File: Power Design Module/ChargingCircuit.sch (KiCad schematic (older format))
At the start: 21 parts, among them J4 USB_B_Micro, J5 Battery Output, SW1 Charge Disable Switch, SW2 Input Current Selection, U3 BQ24072TRGTR

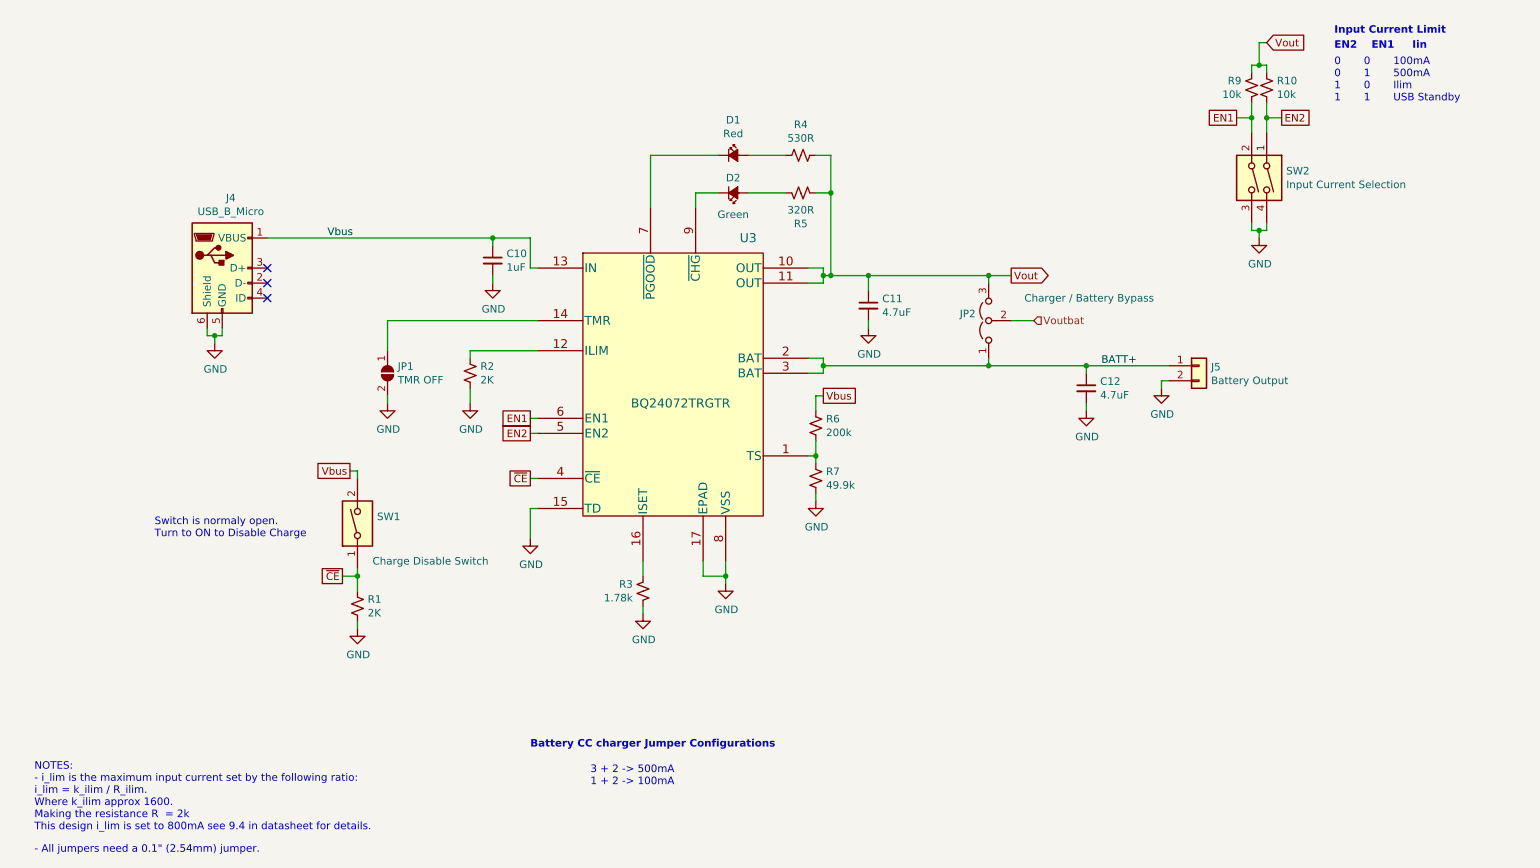
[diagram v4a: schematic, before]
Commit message: Final Power Breakout completed. Headers were used instead of the previous Molex Connectors
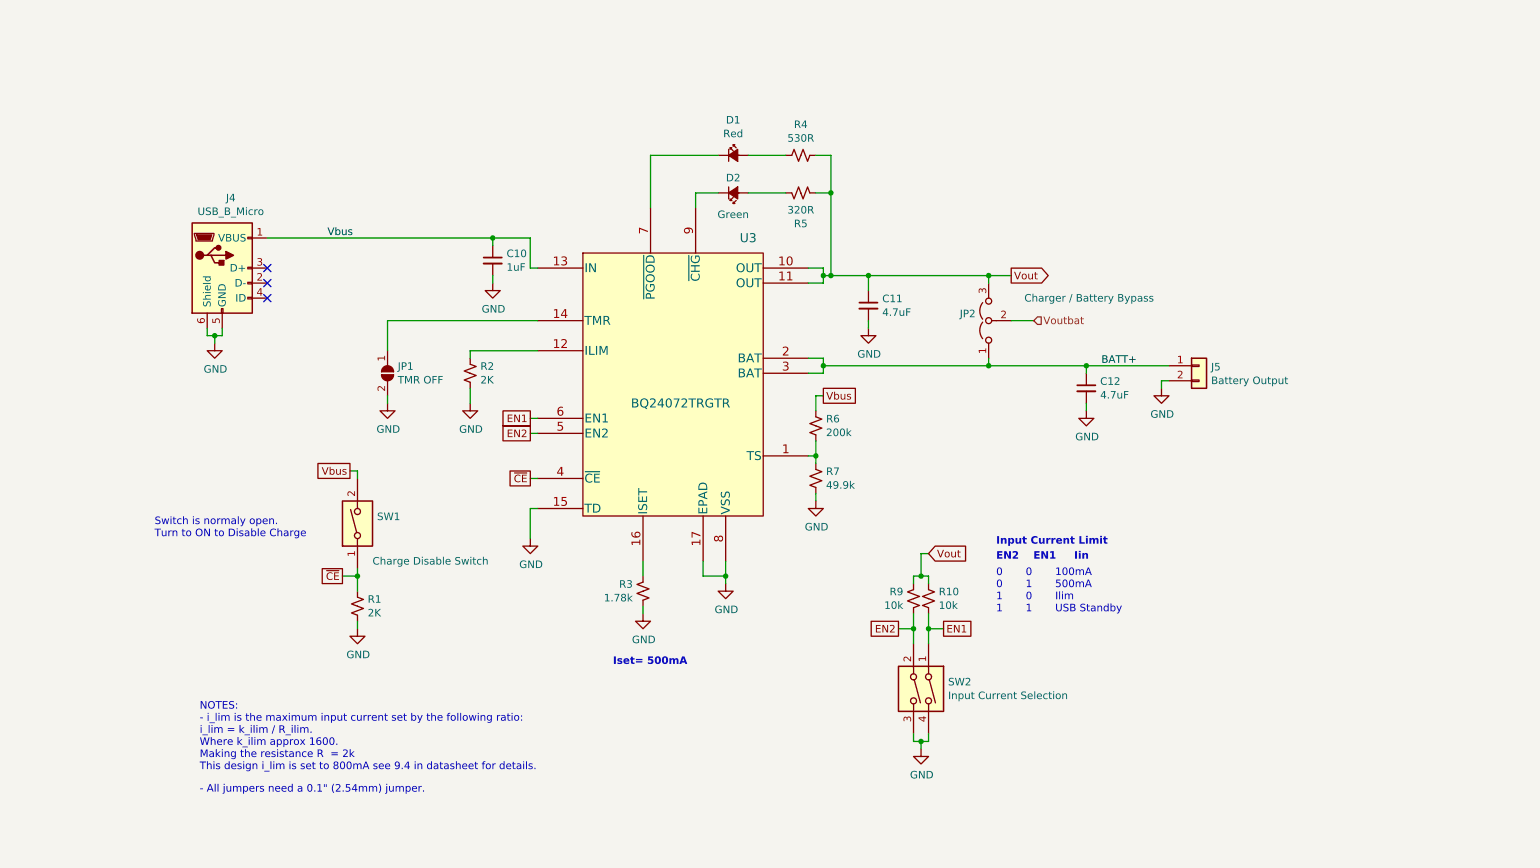
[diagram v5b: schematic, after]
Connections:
- net EN1: now also R10.2, SW2.1; no longer R9.1, SW2.2
- net EN2: now also R9.1, SW2.2; no longer R10.2, SW2.1
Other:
- note added: "Iset= 500mA\n"
- note removed: "3 + 2 -> 500mA\n1 + 2 -> 100mA"
- note removed: "Battery CC charger Jumper Configurations"
- moved on the sheet: R10, R9, SW2
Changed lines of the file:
@@
 $EndComp
-Wire Wire Line
-	5350 2100 5350 2000
-Wire Wire Line
-	5350 2000 5500 2000
 Wire Wire Line
 	5500 1750 5050 1750
@@
 L Switch:SW_DIP_x02 SW2
 U 1 1 5E2D5AAA
-P 9050 1900
-F 0 "SW2" V 9004 2130 50  0000 L CNN
-F 1 "Input Current Selection" V 9095 2130 50  0000 L CNN
-F 2 "Button_Switch_SMD:SW_DIP_SPSTx02_Slide_Copal_CHS-02B_W7.62mm_P1.27mm" H 9050 1900 50  0001 C CNN
-F 3 "~" H 9050 1900 50  0001 C CNN
-F 4 "CVS-02TB" H 9050 1900 50  0001 C CNN "Manfacturing #"
-	1    9050 1900
+P 6800 5300
+F 0 "SW2" V 6754 5530 50  0000 L CNN
+F 1 "Input Current Selection" V 6845 5530 50  0000 L CNN
+F 2 "Button_Switch_SMD:SW_DIP_SPSTx02_Slide_Copal_CHS-02B_W7.62mm_P1.27mm" H 6800 5300 50  0001 C CNN
+F 3 "~" H 6800 5300 50  0001 C CNN
+F 4 "CVS-02TB" H 6800 5300 50  0001 C CNN "Manfacturing #"
+	1    6800 5300
 	0    1    1    0
 $EndComp
-Text GLabel 9150 1000 2    50   Input ~ 0
+Text GLabel 6900 4400 2    50   Input ~ 0
 Vout
-Text GLabel 8950 1500 0    50   UnSpc ~ 0
+Text GLabel 7000 4900 2    50   UnSpc ~ 0
 EN1
-Text GLabel 9250 1500 2    50   UnSpc ~ 0
+Text GLabel 6700 4900 0    50   UnSpc ~ 0
 EN2
 $Comp
 L Device:R_Small_US R9
 U 1 1 5E2E11CE
-P 9050 1300
-F 0 "R9" H 8982 1254 50  0000 R CNN
-F 1 "10k" H 8982 1345 50  0000 R CNN
-F 2 "Resistor_SMD:R_0603_1608Metric_Pad1.05x0.95mm_HandSolder" H 9050 1300 50  0001 C CNN
-F 3 "~" H 9050 1300 50  0001 C CNN
-F 4 "SG73G1JTTD1002D" H 9050 1300 50  0001 C CNN "Manfacturing #"
-	1    9050 1300
+P 6800 4700
+F 0 "R9" H 6732 4654 50  0000 R CNN
+F 1 "10k" H 6732 4745 50  0000 R CNN
+F 2 "Resistor_SMD:R_0603_1608Metric_Pad1.05x0.95mm_HandSolder" H 6800 4700 50  0001 C CNN
+F 3 "~" H 6800 4700 50  0001 C CNN
+F 4 "SG73G1JTTD1002D" H 6800 4700 50  0001 C CNN "Manfacturing #"
+	1    6800 4700
 	1    0    0    1
 $EndComp
@@
 L Device:R_Small_US R10
 U 1 1 5E2E2CB5
-P 9150 1300
-F 0 "R10" H 9218 1346 50  0000 L CNN
-F 1 "10k" H 9218 1255 50  0000 L CNN
-F 2 "Resistor_SMD:R_0603_1608Metric_Pad1.05x0.95mm_HandSolder" H 9150 1300 50  0001 C CNN
-F 3 "~" H 9150 1300 50  0001 C CNN
-F 4 "SG73G1JTTD1002D" H 9150 1300 50  0001 C CNN "Manfacturing #"
-	1    9150 1300
-	1    0    0    -1
-$EndComp
-Wire Wire Line
-	9050 1400 9050 1500
-Wire Wire Line
-	9050 1500 8950 1500
-Wire Wire Line
-	9050 1500 9050 1600
-Connection ~ 9050 1500
-Wire Wire Line
-	9150 1400 9150 1500
-Wire Wire Line
-	9250 1500 9150 1500
-Connection ~ 9150 1500
-Wire Wire Line
-	9150 1500 9150 1600
-Wire Wire Line
-	9050 1200 9050 1150
-Wire Wire Line
-	9050 1150 9100 1150
-Wire Wire Line
-	9150 1150 9150 1200
-Wire Wire Line
-	9150 1000 9100 1000
-Wire Wire Line
-	9100 1000 9100 1150
-Connection ~ 9100 1150
-Wire Wire Line
-	9100 1150 9150 1150
-Wire Wire Line
-	9050 2200 9050 2250
-Wire Wire Line
-	9050 2250 9100 2250
-Wire Wire Line
-	9150 2250 9150 2200
-Wire Wire Line
-	9100 2250 9100 2300
-Connection ~ 9100 2250
-Wire Wire Line
-	9100 2250 9150 2250
+P 6900 4700
+F 0 "R10" H 6968 4746 50  0000 L CNN
+F 1 "10k" H 6968 4655 50  0000 L CNN
+F 2 "Resistor_SMD:R_0603_1608Metric_Pad1.05x0.95mm_HandSolder" H 6900 4700 50  0001 C CNN
+F 3 "~" H 6900 4700 50  0001 C CNN
+F 4 "SG73G1JTTD1002D" H 6900 4700 50  0001 C CNN "Manfacturing #"
+	1    6900 4700
+	1    0    0    -1
+$EndComp
+Wire Wire Line
+	6800 4800 6800 4900
+Wire Wire Line
+	6800 4900 6700 4900
+Wire Wire Line
+	6800 4900 6800 5000
+Connection ~ 6800 4900
+Wire Wire Line
+	6900 4800 6900 4900
+Wire Wire Line
+	7000 4900 6900 4900
+Connection ~ 6900 4900
+Wire Wire Line
+	6900 4900 6900 5000
+Wire Wire Line
+	6800 4600 6800 4550
+Wire Wire Line
+	6800 4550 6850 4550
+Wire Wire Line
+	6900 4550 6900 4600
+Wire Wire Line
+	6900 4400 6850 4400
+Wire Wire Line
+	6850 4400 6850 4550
+Connection ~ 6850 4550
+Wire Wire Line
+	6850 4550 6900 4550
+Wire Wire Line
+	6800 5600 6800 5650
+Wire Wire Line
+	6800 5650 6850 5650
+Wire Wire Line
+	6900 5650 6900 5600
+Wire Wire Line
+	6850 5650 6850 5700
+Connection ~ 6850 5650
+Wire Wire Line
+	6850 5650 6900 5650
 $Comp
 L power:GND #PWR0114
 U 1 1 5E2FEC35
-P 9100 2300
-F 0 "#PWR0114" H 9100 2050 50  0001 C CNN
-F 1 "GND" H 9105 2127 50  0000 C CNN
-F 2 "" H 9100 2300 50  0001 C CNN
-F 3 "" H 9100 2300 50  0001 C CNN
-	1    9100 2300
-	1    0    0    -1
-$EndComp
-Text Notes 9600 1400 0    50   ~ 0
+P 6850 5700
+F 0 "#PWR0114" H 6850 5450 50  0001 C CNN
+F 1 "GND" H 6855 5527 50  0000 C CNN
+F 2 "" H 6850 5700 50  0001 C CNN
+F 3 "" H 6850 5700 50  0001 C CNN
+	1    6850 5700
+	1    0    0    -1
+$EndComp
+Text Notes 7350 4800 0    50   ~ 0
 0       0       100mA\n0       1       500mA\n1       0       Ilim\n1       1       USB Standby
-Text Notes 9600 1050 0    50   ~ 10
+Text Notes 7350 4450 0    50   ~ 10
 EN2    EN1     Iin
 Text Label 8050 3150 0    50   ~ 0
@@
 Wire Wire Line
 	3850 3050 4300 3050
-Text Notes 950  6250 0    50   ~ 0
-NOTES:\n- i_lim is the maximum input current set by the following ratio:\ni_lim = k_ilim / R_ilim.\nWhere k_ilim approx 1600. \nMaking the resistance R  = 2k\nThis design i_lim is set to 800mA see 9.4 in datasheet for details.
 Text GLabel 3000 4550 0    50   UnSpc ~ 0
 ~CE
@@
 Wire Wire Line
 	5000 4750 5000 4800
-Text Notes 4250 5700 0    50   ~ 10
-Battery CC charger Jumper Configurations
-Text Notes 4650 5950 0    50   ~ 0
-3 + 2 -> 500mA\n1 + 2 -> 100mA
 $Comp
 L power:GND #PWR0119
@@
 Wire Wire Line
 	5550 4550 5550 4600
-Text Notes 9600 950  0    50   ~ 10
+Text Notes 7350 4350 0    50   ~ 10
 Input Current Limit
 NoConn ~ 2500 2500
@@
 Text Notes 1750 4300 0    50   ~ 0
 Switch is normaly open.\nTurn to ON to Disable Charge
-Text Notes 950  6400 0    50   ~ 0
+Text Notes 2050 6000 0    50   ~ 0
 - All jumpers need a 0.1" (2.54mm) jumper.
 Wire Wire Line
@@
 	7300 2550 7450 2550
 Connection ~ 7300 2550
+Wire Wire Line
+	5350 2000 5500 2000
+Wire Wire Line
+	5350 2100 5350 2000
+Text Notes 4800 5150 0    50   ~ 10
+Iset= 500mA\n
+Text Notes 2050 5850 0    50   ~ 0
+NOTES:\n- i_lim is the maximum input current set by the following ratio:\ni_lim = k_ilim / R_ilim.\nWhere k_ilim approx 1600. \nMaking the resistance R  = 2k\nThis design i_lim is set to 800mA see 9.4 in datasheet for details.
 $EndSCHEMATC
